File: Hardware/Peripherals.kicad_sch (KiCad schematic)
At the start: 21 parts, among them J3 0532610271, J4 Conn_Coaxial, J5 B8B-PH-SM4-TB, U4 DRV2605LDGS, U5 BNO055, U6 TESEO-LIV3F, U7 BGA725L6, U8 B4327

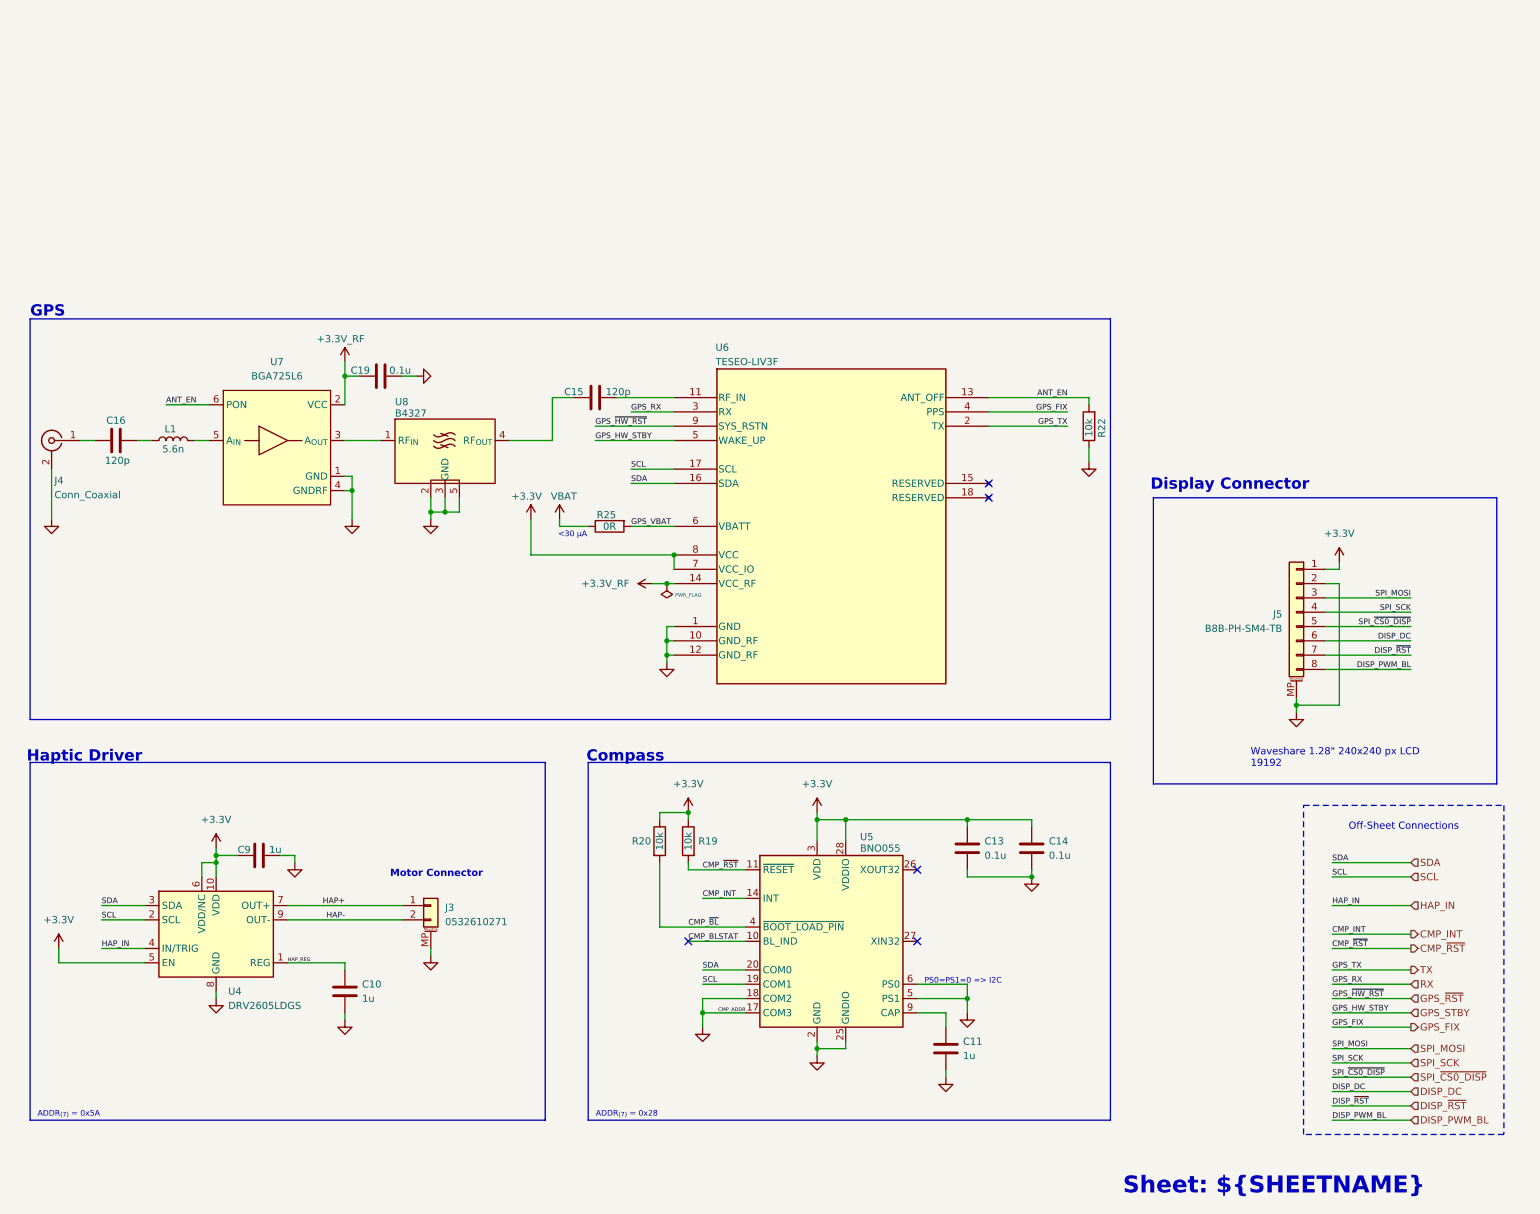
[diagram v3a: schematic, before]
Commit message: sch: change GPS to Adafruit PA1616D
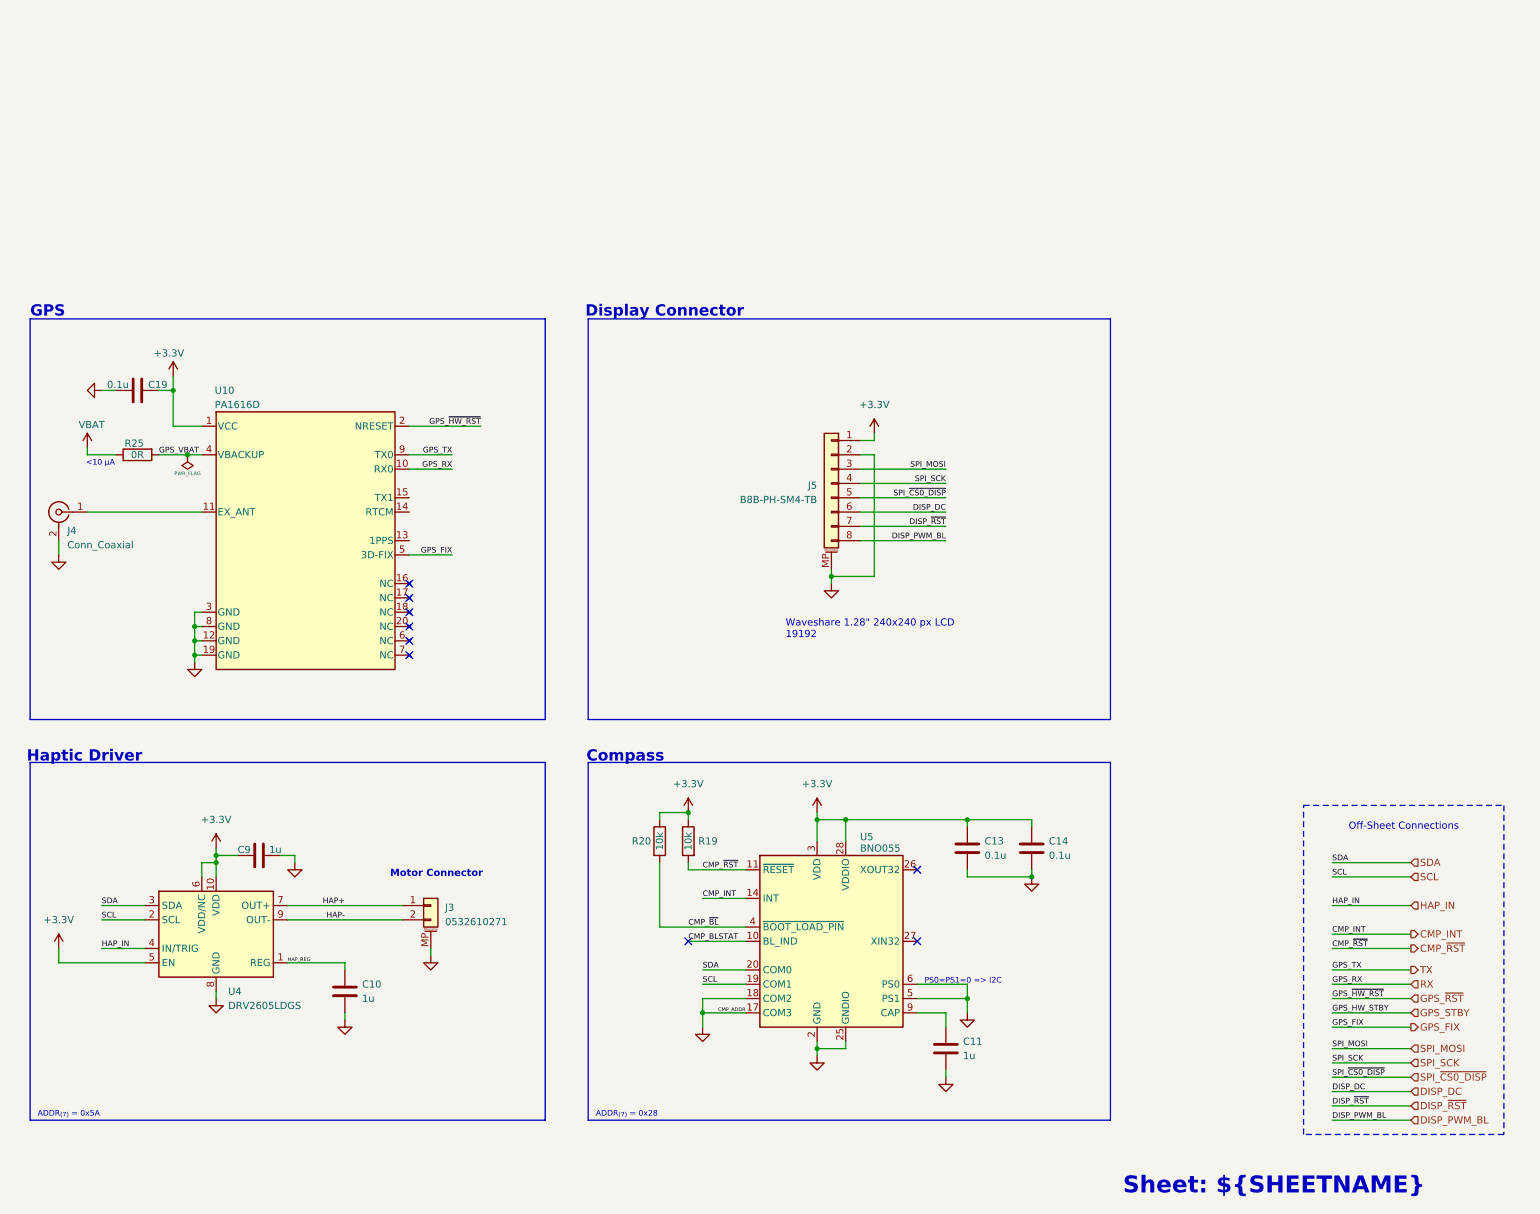
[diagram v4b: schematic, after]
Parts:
- removed C15, C16: 120p, Capacitor_SMD:C_0402_1005Metric, symbol Device:C
- removed L1: 5.6n, Inductor_SMD:L_0402_1005Metric, symbol Device:L
- removed R22: 10k, Resistor_SMD:R_0603_1608Metric, symbol Device:R
- removed U6: TESEO-LIV3F, LCC-18_9P7X10P1_STM, symbol 2025-06-15_18-00-59:TESEO-LIV3F
- removed U7: BGA725L6, Symbols:BGA-6_2x3_0.8x1.2mm, symbol 2025-06-15_18-00-59:BGA725L6
- removed U8: B4327, Symbols:SOIC-5 B4327, symbol 2025-06-15_18-00-59:B4327
- added U10: PA1616D, LCC-18_9P7X10P1_STM, symbol 2025-06-15_18-00-59:PA1616D
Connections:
- net +3.3V_RF is gone; now on net +3.3V: C19.1
- net +3.3V: now also U10.1 (VCC)
- net GND: now also U10.12 (GND), U10.19 (GND), U10.3 (GND), U10.8 (GND)
- net GPS_FIX: now also U10.5 (3D-FIX)
- net GPS_VBAT: now also U10.4 (VBACKUP)
- net GPS_~{RST}: now also U10.2 (NRESET)
- net RX: now also U10.10 (RX0)
- net TX: now also U10.9 (TX0)
- net at J4.1 (In): now also U10.11 (EX_ANT)
- no-connect marks 5 -> 9
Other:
- note added: "<10 μA"
- note removed: "<30 μA"
- moved on the sheet: C19, J4, J5, R25

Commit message: sch: updates
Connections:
- no-connect marks 9 -> 12
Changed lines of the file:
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@@
 	(title_block
 		(title "${TITLE}")
-		(date "2025-04-06")
+		(date "2025-08-29")
 		(rev "${REVISION}")
 		(company "${COMPANY}")
@@
 	)
 	(no_connect
+		(at 87.63 54.61)
+	)
+	(no_connect
 		(at 87.63 72.39)
 	)
@@
 	)
 	(no_connect
+		(at 87.63 59.69)
+	)
+	(no_connect
 		(at 87.63 77.47)
 	)
@@
 	)
 	(no_connect
+		(at 87.63 52.07)
+	)
+	(no_connect

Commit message: sch/pcb: add and link footprint for PA1616D
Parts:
- U10: footprint LCC-18_9P7X10P1_STM -> TESO-LIV3F:PA1616D
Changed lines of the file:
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@@
 			)
 		)
-		(property "Footprint" "LCC-18_9P7X10P1_STM"
+		(property "Footprint" "TESO-LIV3F:PA1616D"
 			(at 58.42 27.94 0)
 			(effects

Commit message: pcb: final route + cleanup. sch: dnp gps conn.
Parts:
- J4: now not fitted; now left out of the parts list
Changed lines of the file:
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@@
 		(unit 1)
 		(exclude_from_sim no)
-		(in_bom yes)
+		(in_bom no)
 		(on_board yes)
-		(dnp no)
+		(dnp yes)
 		(property "Reference" "J4"
 			(at 26.924 57.912 0)
